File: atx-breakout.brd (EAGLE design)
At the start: 160 x 100 mm, 74 parts, among them Q1 IRF9530, Q2 IRF9530, Q3 IRF9530, Q4 IRF9530, Q5 IRF9530, Q6 IRF9530, T1 2N3904, T2 2N3904, T3 2N3904, T4 2N3904, T5 2N3904, T6 2N3904, X10 MA02-1JC, X12 XT30-J, X13 MA02-1JC, X15 XT30-J, X16 MA02-1JC, X2 XT30-J, X3 MA02-1JC, X4 XT30-J, X5 MA02-1JC, X6 XT30-J, X7 MA02-1JC, X9 XT30-J

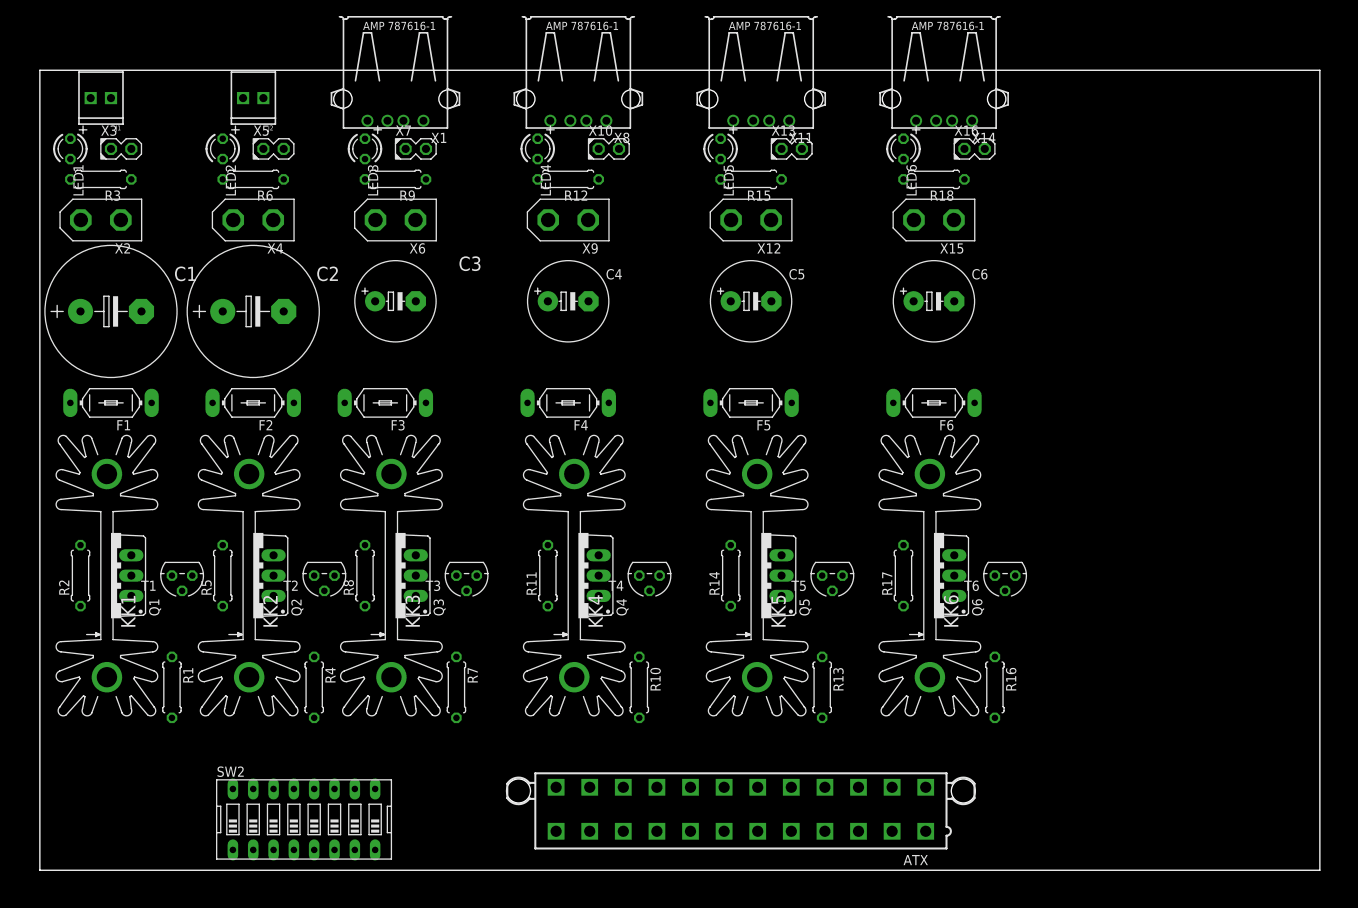
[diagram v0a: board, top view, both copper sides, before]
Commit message: Added 3v3, control header, fan control headers, extra room for filter cap
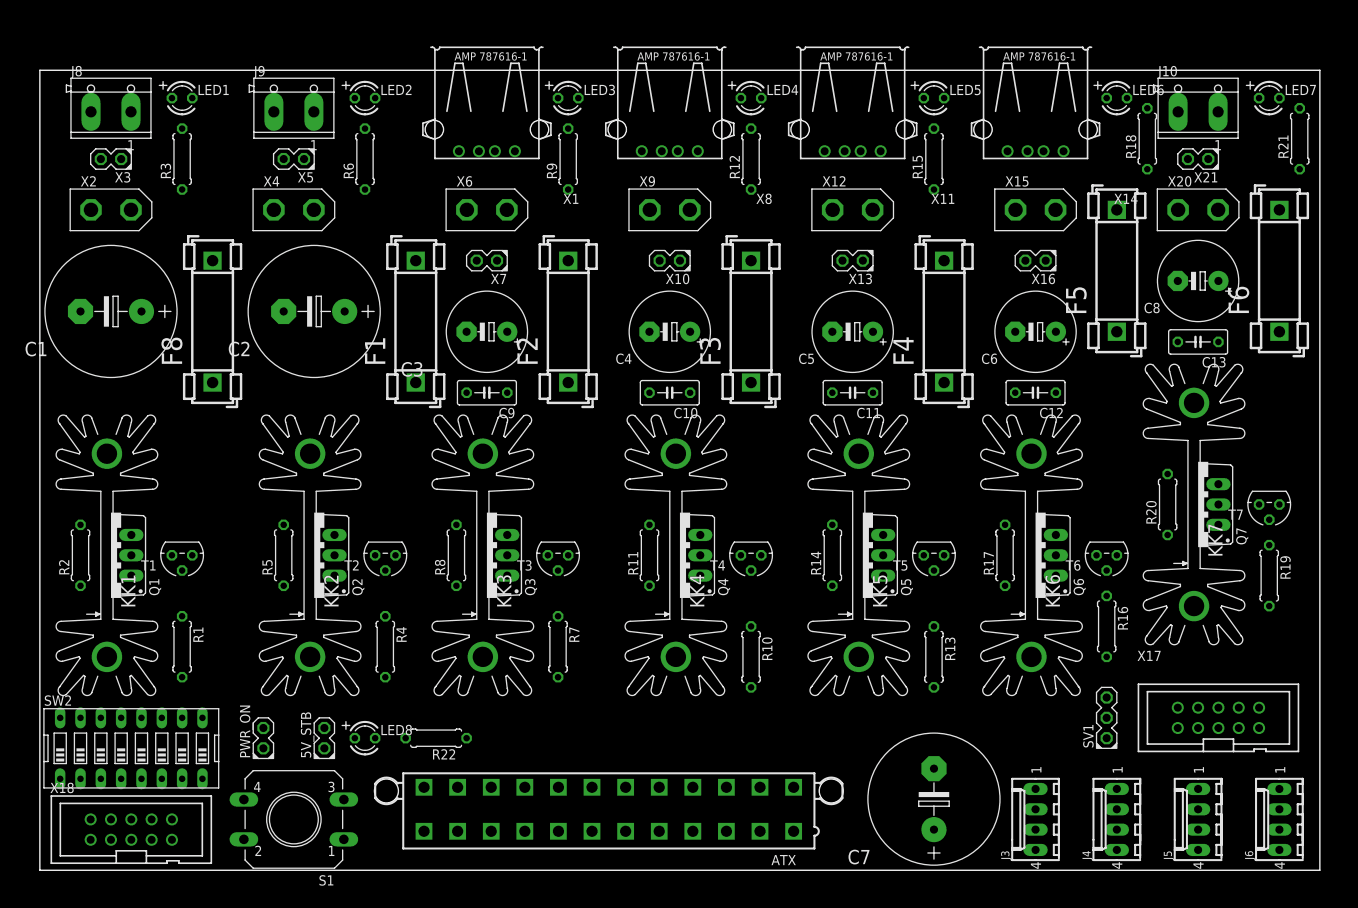
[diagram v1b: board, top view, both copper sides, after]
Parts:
- removed J1, J2: (no value), SparkFun-Connectors:1X02_2.54_SCREWTERM
- added 5V_STB, PWR_ON, X21: MA02-1JC, joakim:MA02-1J
- added C10, C11, C12, C13, C9: (no value), rcl:C050-030X075
- added C7: 2200uF, rcl:E7,5-16
- added C8: 1000uF, rcl:E5-10,5
- added F8: FUSE, fuse:FUSE_HOLDER_5X20MM
- added J10, J8, J9: CON_TERMINAL_BLOCK_02-5MM, dp_devices.v6:TERMINAL_BLOCK_2P_5
- added J3, J4, J5, J6: Molex KK 47053-1000, con-molex:6410-04
- added KK7: SK104-PAD, heatsink:SK104-PAD
- added LED7, LED8: (no value), joakim:LED3MM
- added Q7: IRF9530, transistor-power:TO220BV
- added R19, R20: 1k, rcl:0207/7
- added R21: 150R, rcl:0207/7
- added R22: 220R, rcl:0207/7
- added S1: (no value), joakim:PUSHBUTTON_12MM
- added SV1: (no value), joakim:MA03-1J
- added T7: 2N3904, transistor:TO92
- added X17, X18: CONN-IDC-10PS, joakim:CONN-IDC10P-S
- added X20: XT30-J, joakim:XT30-J
- F1, F2, F3, F4, F5, F6: value (none) -> FUSE; device fuse:LITTLEFUSE -> fuse:FUSE_HOLDER_5X20MM
- R12, R15, R18, R9: value 1k -> 220R
- R3, R6: value 1k -> 560R
- moved F4 47.1 mm to (113.0, 61.0), turned to 90 degrees
- moved F5 46.6 mm to (134.6, 67.3), turned to 90 degrees
- moved F3 45.8 mm to (88.9, 61.0), turned to 90 degrees
- moved F6 44.1 mm to (154.9, 67.3), turned to 90 degrees
- moved F2 39.5 mm to (66.0, 61.0), turned to 90 degrees
- moved F1 38.2 mm to (47.0, 61.0), turned to 90 degrees
- moved LED4 27.4 mm to (88.9, 96.5), turned to 0 degrees
- moved LED5 27.4 mm to (111.8, 96.5), turned to 0 degrees
- moved LED6 27.4 mm to (134.6, 96.5), turned to 0 degrees
- moved R18 27.1 mm to (138.4, 91.4), turned to 90 degrees
- moved LED3 26.2 mm to (66.0, 96.5), turned to 0 degrees
- moved SW2 23.3 mm to (11.4, 15.2)
- moved R12 23.0 mm to (88.9, 88.9), turned to 90 degrees
- moved R15 23.0 mm to (111.8, 88.9), turned to 90 degrees
- moved R9 21.7 mm to (66.0, 88.9), turned to 90 degrees
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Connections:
- new net +12V/1: ATX.10, C7.+, J3.2, J4.2, J5.2, J6.2, Q1.S, R2.2
- new net +12V/2: ATX.11, Q2.S, R5.2
- new net +3V3/1: ATX.1, Q7.S, R20.2
- new net +3V3/2: ATX.2
- new net +3V3/3: ATX.12
- new net +3V3/4: ATX.13
- new net FAN1_CTRL: J3.4, X17.2
- new net FAN1_SENSE: J3.3, X17.1
- new net FAN2_CTRL: J4.4, X17.4
- new net FAN2_SENSE: J4.3, X17.3
- new net FAN3_CTRL: J5.4, X17.6
- new net FAN3_SENSE: J5.3, X17.5
- new net FAN4_CTRL: J6.4, X17.8
- new net FAN4_SENSE: J6.3, X17.7
- new net N$32: SV1.2, X17.9
- new net N$33: R19.1, T7.2
- new net N$34: Q7.G, R20.1, T7.1
- new net N$35: C13.1, C8.+, F6.2, J10.1, LED7.A, X20.1, X21.1
- new net N$36: LED7.K, R21.2
- new net N$37: F6.1, Q7.D
- new net PWR_CTRL_3V1: R19.2
- net +5V/1: now also SV1.3; no longer ATX.1, ATX.10, ATX.11, ATX.12, ATX.13, ATX.2, Q2.S, R5.2
- net +5V_STB: now also 5V_STB.1, LED8.A, PWR_ON.1, S1.2, SV1.1
- net GND: now also 5V_STB.2, C10.2, C11.2, C12.2, C13.2, C7.-, C8.-, C9.2, J10.2, J3.1, J4.1, J5.1, J6.1, J8.2, J9.2, R21.1, R22.1, T7.3, X17.10, X20.2, X21.2; no longer J1.P2, J2.P2
- net N$11: now also F1.1; no longer F2.1
- net N$14: now also C9.1, F2.2; no longer F3.2
- net N$16: now also F2.1; no longer F3.1
- net N$19: now also C10.1, F3.2; no longer F4.2
- net N$21: now also F3.1; no longer F4.1
- net N$24: now also C11.1, F4.2; no longer F5.2
- net N$26: now also F4.1; no longer F5.1
- net N$29: now also C12.1, F5.2; no longer F6.2
- net N$3: now also LED8.K, R22.2; no longer Q1.S, R2.2
- net N$31: now also F5.1; no longer F6.1
- net N$4: now also F8.2, J8.1; no longer F1.2, J1.P1
- net N$6: now also F8.1; no longer F1.1
- net N$9: now also F1.2, J9.1; no longer F2.2, J2.P1
- net PWR_CTRL_12V1: now also X18.1
- net PWR_CTRL_12V2: now also X18.2
- net PWR_CTRL_5V1: now also X18.3
- net PWR_CTRL_5V2: now also X18.4
- net PWR_CTRL_5V3: now also X18.5
- net PWR_CTRL_5V4: now also X18.6
- net PWR_ON: now also PWR_ON.2, S1.4

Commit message: More cleanup, made room for screws etc
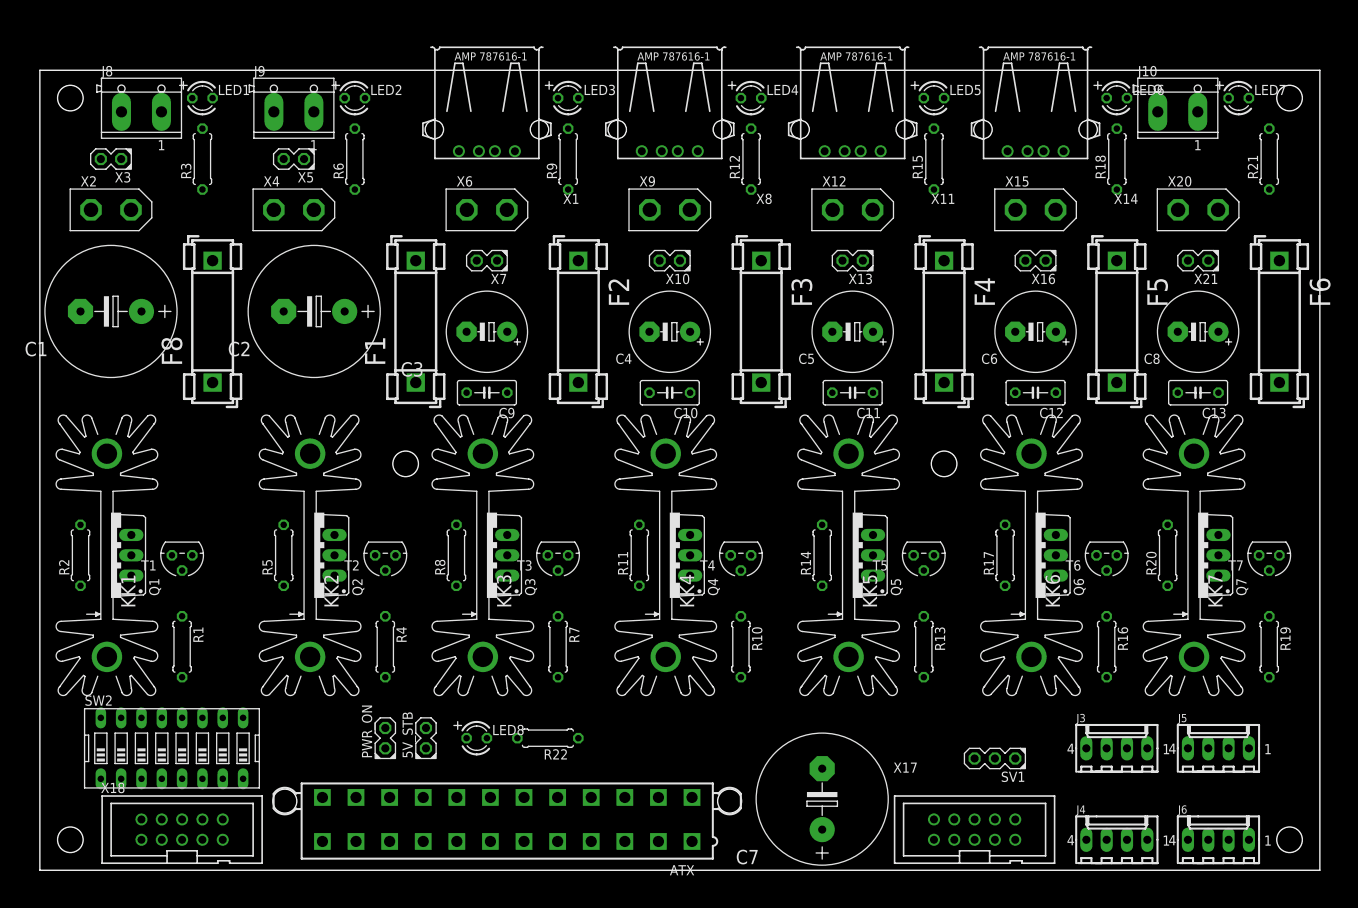
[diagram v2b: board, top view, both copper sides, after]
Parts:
- removed S1: (no value), joakim:PUSHBUTTON_12MM
- moved X17 33.5 mm to (116.8, 5.08)
- moved F2 15.3 mm to (67.3, 76.2), turned to 270 degrees
- moved F3 15.3 mm to (90.2, 76.2), turned to 270 degrees
- moved F4 15.2 mm to (113.0, 76.2), turned to 270 degrees
- moved PWR_ON 15.2 mm to (43.2, 17.8)
- moved SV1 14.9 mm to (119.4, 14.0), turned to 180 degrees
- moved C7 14.0 mm to (97.8, 8.89)
- moved LED8 14.0 mm to (54.6, 16.5)
- moved R22 14.0 mm to (63.5, 16.5)
- moved J3 13.5 mm to (134.6, 15.2), turned to 0 degrees
- moved ATX 12.8 mm to (58.4, 6.35)
- moved X21 12.7 mm to (143.5, 76.2)
- moved 5V_STB 12.7 mm to (48.3, 17.8)
- moved J5 9.25 mm to (147.3, 15.2), turned to 0 degrees
- moved F5 8.89 mm to (134.6, 76.2), turned to 270 degrees
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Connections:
- net +5V/1: now also X18.9
- net +5V_STB: no longer S1.2
- net GND: now also X18.10
- net PWR_CTRL_12V2: now also SW2.2
- net PWR_CTRL_3V1: now also SW2.7, X18.7
- net PWR_CTRL_5V1: now also SW2.3
- net PWR_CTRL_5V2: now also SW2.4
- net PWR_CTRL_5V3: now also SW2.5
- net PWR_CTRL_5V4: now also SW2.6
- net PWR_ON: no longer S1.4

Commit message: Everything routed, but need to rething GND
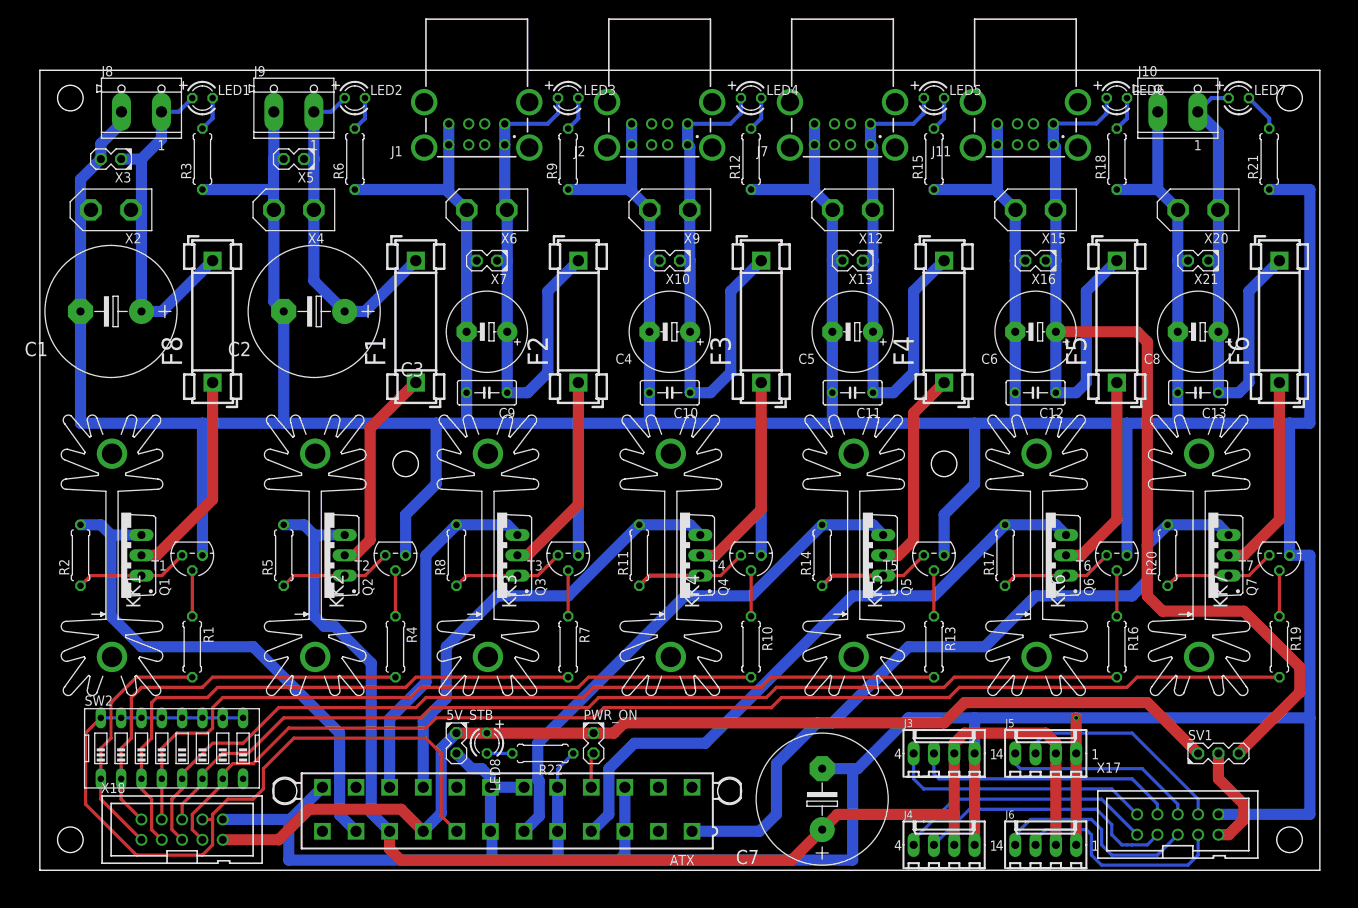
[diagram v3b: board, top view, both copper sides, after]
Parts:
- removed X1, X11, X14, X8: (no value), con-amp:USB
- added J1, J11, J2, J7: 61400826021, Wurth_Connectors_WR-USB:61400826021
- moved SV1 27.9 mm to (147.3, 14.6), turned to 0 degrees
- moved PWR_ON 26.2 mm to (69.2, 14.6), turned to 270 degrees
- moved X17 25.4 mm to (142.2, 5.71)
- moved J3 21.6 mm to (113.0, 14.6)
- moved J4 21.6 mm to (113.0, 3.17)
- moved J5 21.6 mm to (125.7, 14.6)
- moved J6 21.6 mm to (125.7, 3.17)
- moved F2 15.2 mm to (67.3, 61.0), turned to 90 degrees
- moved F3 15.2 mm to (90.2, 61.0), turned to 90 degrees
- moved F4 15.2 mm to (113.0, 61.0), turned to 90 degrees
- moved F5 15.2 mm to (134.6, 61.0), turned to 90 degrees
- moved F6 15.2 mm to (154.9, 61.0), turned to 90 degrees
- moved 5V_STB 4.96 mm to (52.1, 14.6), turned to 270 degrees
- moved R22 2.01 mm to (62.9, 14.6)
- moved LED8 1.42 mm to (55.9, 15.9), turned to 270 degrees
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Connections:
- removed net N$29: C12.1, C6.+, F5.2, LED6.A, X14.1, X15.1, X16.1
- new net SW5V1: C12.1, C6.+, F5.2, J11.1, J11.5, LED6.A, SV1.3, X15.2, X16.1
- net +12V/1: now also Q2.S, R5.2; no longer Q1.S, R2.2
- net +12V/2: now also Q1.S, R2.2; no longer Q2.S, R5.2
- net +5V/1: now also Q6.S, R17.2; no longer Q3.S, R8.2, SV1.3, X18.9
- net +5V/2: now also Q5.S, R14.2; no longer Q4.S, R11.2
- net +5V/3: now also Q4.S, R11.2; no longer Q5.S, R14.2
- net +5V/4: now also Q3.S, R8.2; no longer Q6.S, R17.2
- net +5V_STB: now also X18.9
- net FAN1_SENSE: now also X17.4; no longer X17.1
- net FAN2_CTRL: now also X17.1; no longer X17.4
- net FAN3_SENSE: now also X17.8; no longer X17.5
- net FAN4_CTRL: now also X17.5; no longer X17.8
- net GND: now also J1.4, J1.8, J11.4, J11.8, J2.4, J2.8, J7.4, J7.8, X12.1, X15.1, X2.1, X20.1, X4.1, X6.1, X9.1; no longer X1.4, X11.4, X12.2, X14.4, X15.2, X2.2, X20.2, X4.2, X6.2, X8.4, X9.2
- net N$14: now also J1.1, J1.5, X6.2; no longer X1.1, X6.1
- net N$19: now also J2.1, J2.5, X9.2; no longer X8.1, X9.1
- net N$24: now also J7.1, J7.5, X12.2; no longer X11.1, X12.1
- net N$35: now also X20.2; no longer X20.1
- net N$4: now also X2.2; no longer X2.1
- net N$9: now also X4.2; no longer X4.1
- net PWR_GOOD: now also SW2.10, SW2.11, SW2.12, SW2.13, SW2.14, SW2.15, SW2.16, SW2.9, X18.8
- net PWR_ON: no longer SW2.10, SW2.11, SW2.12, SW2.13, SW2.14, SW2.15, SW2.16, SW2.9
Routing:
- net GND: track 0.00 -> 926.2 mm, vias 0 -> 1
- net +12V/1: track 0.00 -> 164.7 mm
- net PWR_CTRL_3V1: track 0.00 -> 147.4 mm
- net SW5V1: track 0.00 -> 145.7 mm
- net +5V_STB: track 0.00 -> 138.7 mm
- net PWR_CTRL_5V4: track 0.00 -> 126.1 mm
- net PWR_CTRL_5V3: track 0.00 -> 108.3 mm
- net PWR_GOOD: track 0.00 -> 98.8 mm
- net +3V3/1: track 0.00 -> 89.8 mm
- net PWR_CTRL_5V2: track 0.00 -> 87.7 mm
- net +5V/1: track 0.00 -> 79.1 mm
- net PWR_CTRL_5V1: track 0.00 -> 72.1 mm
- net +5V/2: track 0.00 -> 66.9 mm
- net +12V/2: track 0.00 -> 66.1 mm
- net N$24: track 0.00 -> 65.8 mm
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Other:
- board text added: "Separate GNDs per lane?"
- board text added: "Should 10 and 11 be routed down and around instead?"
